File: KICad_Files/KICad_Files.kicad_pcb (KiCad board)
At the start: 2 copper layers, 30 x 34 mm, 48 parts, among them J1 Conn_01x03_Pin, J10 Conn_01x03_MountingPin, J2 Conn_01x03_Pin, J3 Conn_01x06, J4 Conn_01x06, J5 Conn_01x03_Pin, J6 Conn_01x02_Pin, J7 USB_C_Receptacle_USB2.0_16P, J8 Conn_01x03_MountingPin, J9 Conn_01x03_MountingPin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

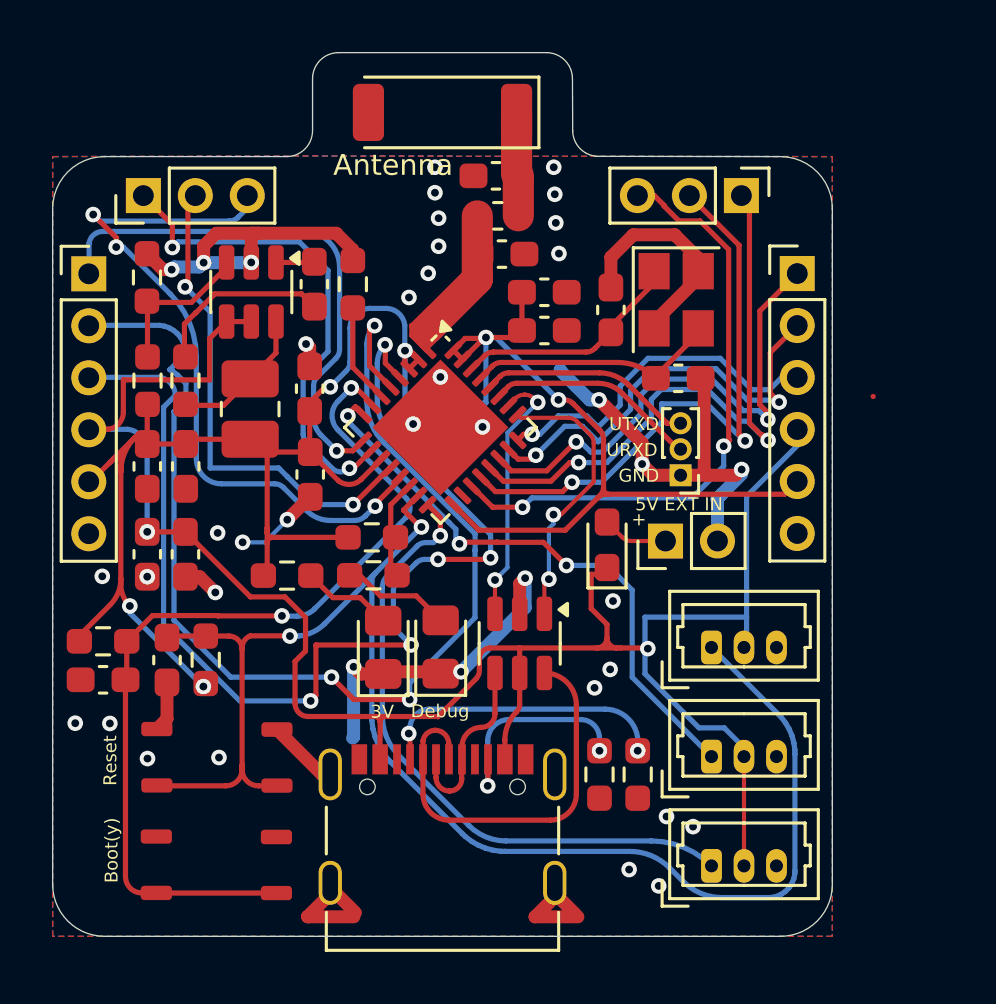
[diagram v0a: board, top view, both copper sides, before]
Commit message: Changed from 3 to 2 connector because of ESP32-C3 Limitations
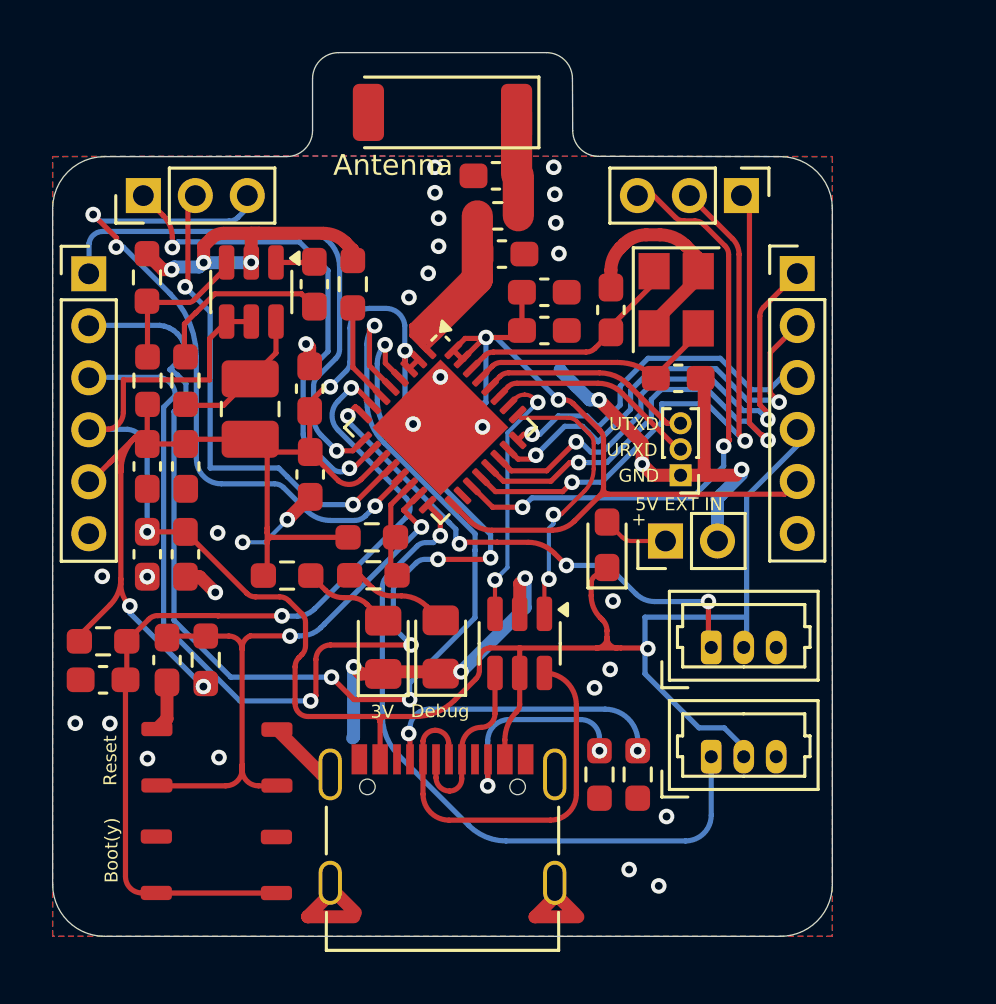
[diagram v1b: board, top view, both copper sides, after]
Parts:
- removed J8: Conn_01x03_MountingPin, Connector_Molex:Molex_PicoBlade_53047-0310_1x03_P1.25mm_Vertical
- moved J9 4.20 mm to (117.1, 103.3)
- moved J10 4.20 mm to (117.1, 107.5)
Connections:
- net /LED3 renamed /Boot
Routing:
- net /Boot: track 60.0 -> 24.3 mm
- net +5V: track 79.1 -> 73.9 mm
- net /LED2: track 22.9 -> 20.0 mm, vias 3 -> 4
- net /LED1: track 24.7 -> 27.2 mm
- net GND: track 74.1 -> 73.8 mm, vias 40 -> 39
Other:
- board text removed: "GPIO9"

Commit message: Switched the pi-filter components to 0402 size and changed the values
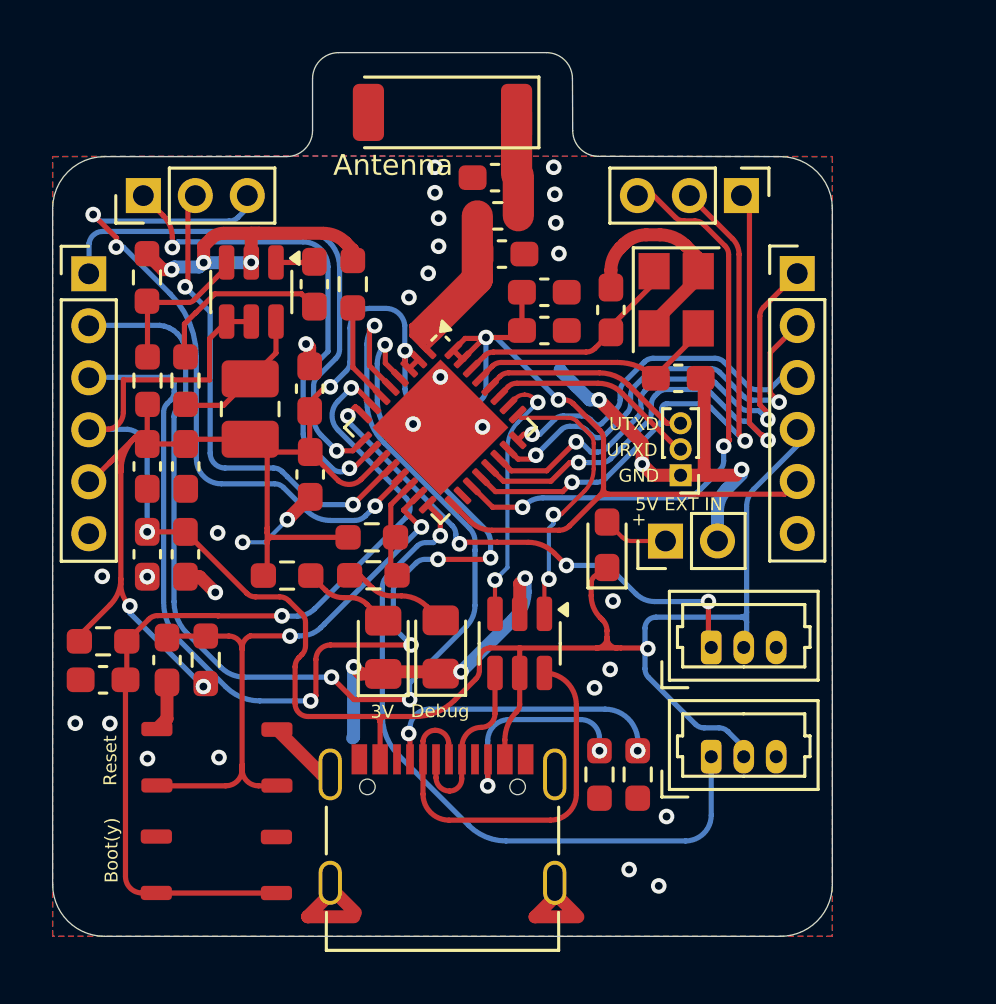
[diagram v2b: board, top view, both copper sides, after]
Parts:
- moved C4 0.08 mm to (108.8, 85.2)
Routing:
- net /GPIO 1: track 45.8 -> 44.9 mm

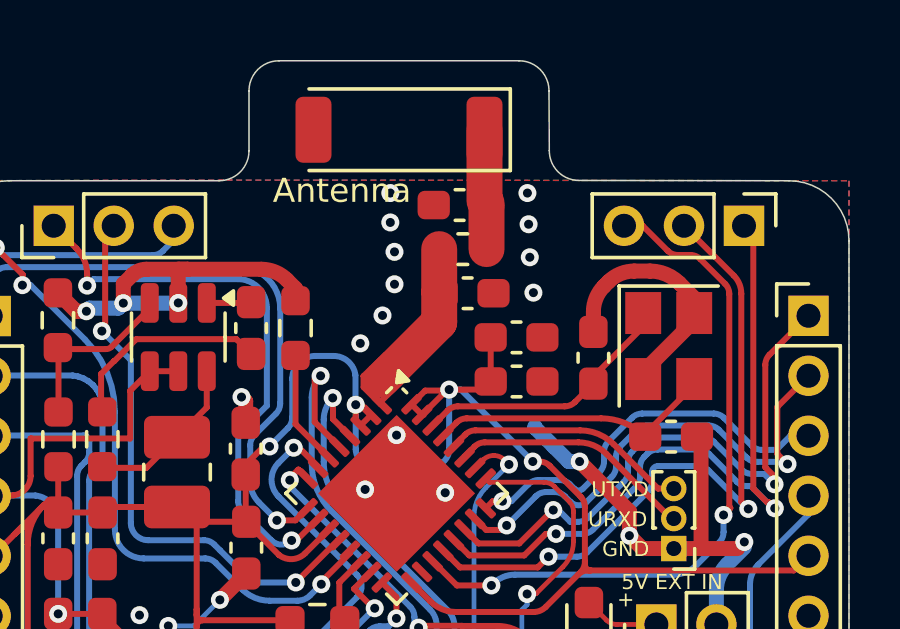
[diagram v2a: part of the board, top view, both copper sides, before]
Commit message: Switched crystal size and changed GPIO02 to be pulled high instead of low
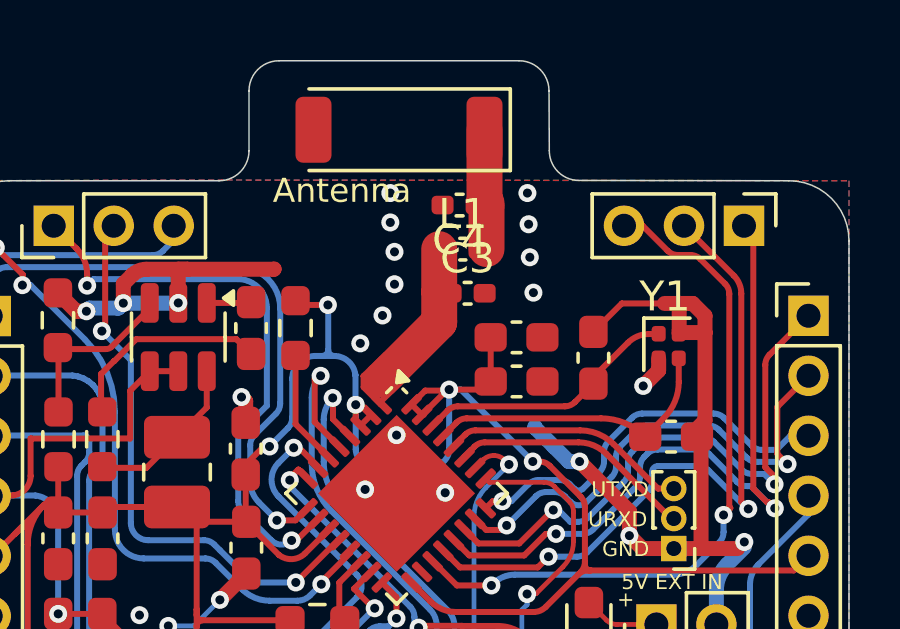
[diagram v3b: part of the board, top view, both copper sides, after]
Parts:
- C3, C4: value 3p3 -> 1p2; footprint Capacitor_SMD:C_0603_1608Metric_Pad1.08x0.95mm_HandSolder -> Capacitor_SMD:C_0402_1005Metric_Pad0.74x0.62mm_HandSolder
- L1: value 2n2 -> 3n9; footprint Inductor_SMD:L_0603_1608Metric -> Inductor_SMD:L_0402_1005Metric_Pad0.77x0.64mm_HandSolder
- Y1: footprint Crystal:Crystal_SMD_3225-4Pin_3.2x2.5mm -> Crystal:Crystal_SMD_1210-4Pin_1.2x1.0mm
- turned Y1 to 0 degrees
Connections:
- R6 pad 1: GND -> +3.3V
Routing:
- net +3.3V: track 88.1 -> 91.4 mm, vias 6 -> 7
- net GND: track 73.4 -> 74.5 mm, vias 39 -> 40

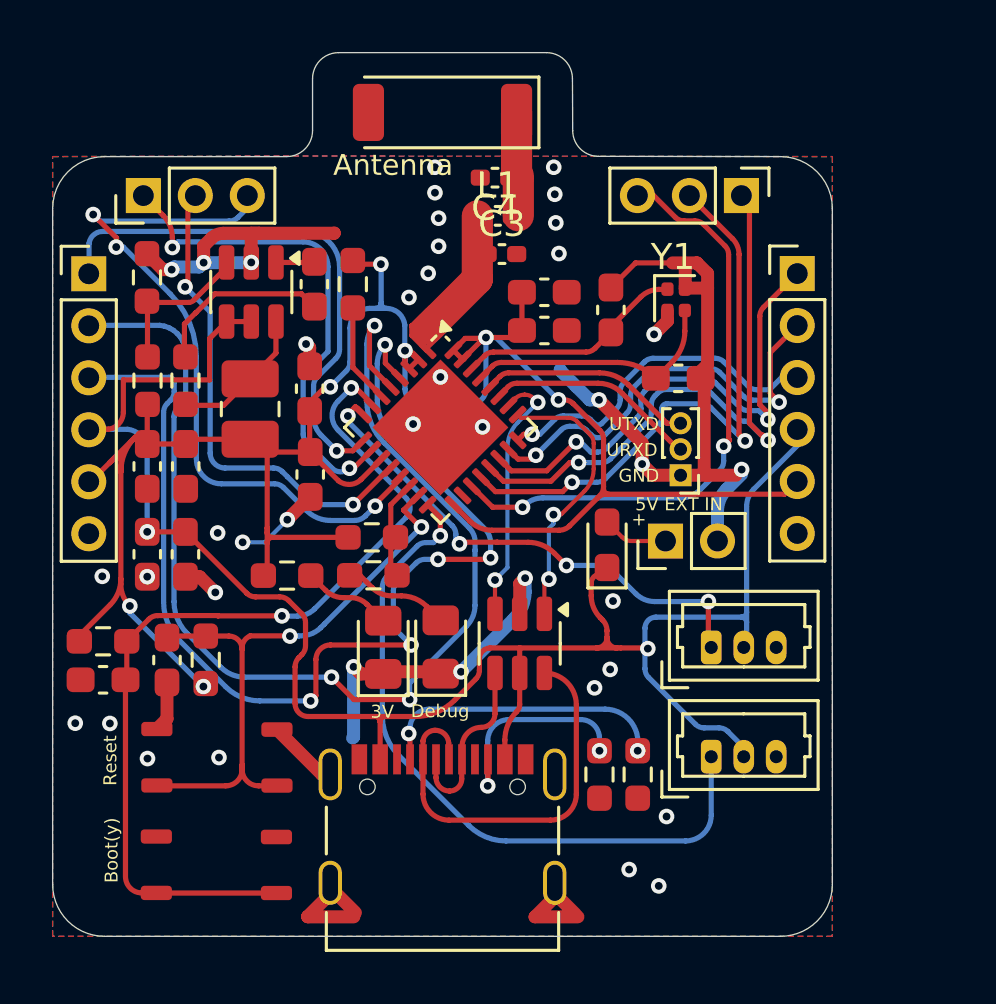
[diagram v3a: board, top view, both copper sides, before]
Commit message: fixed ground plane issues with the antenna
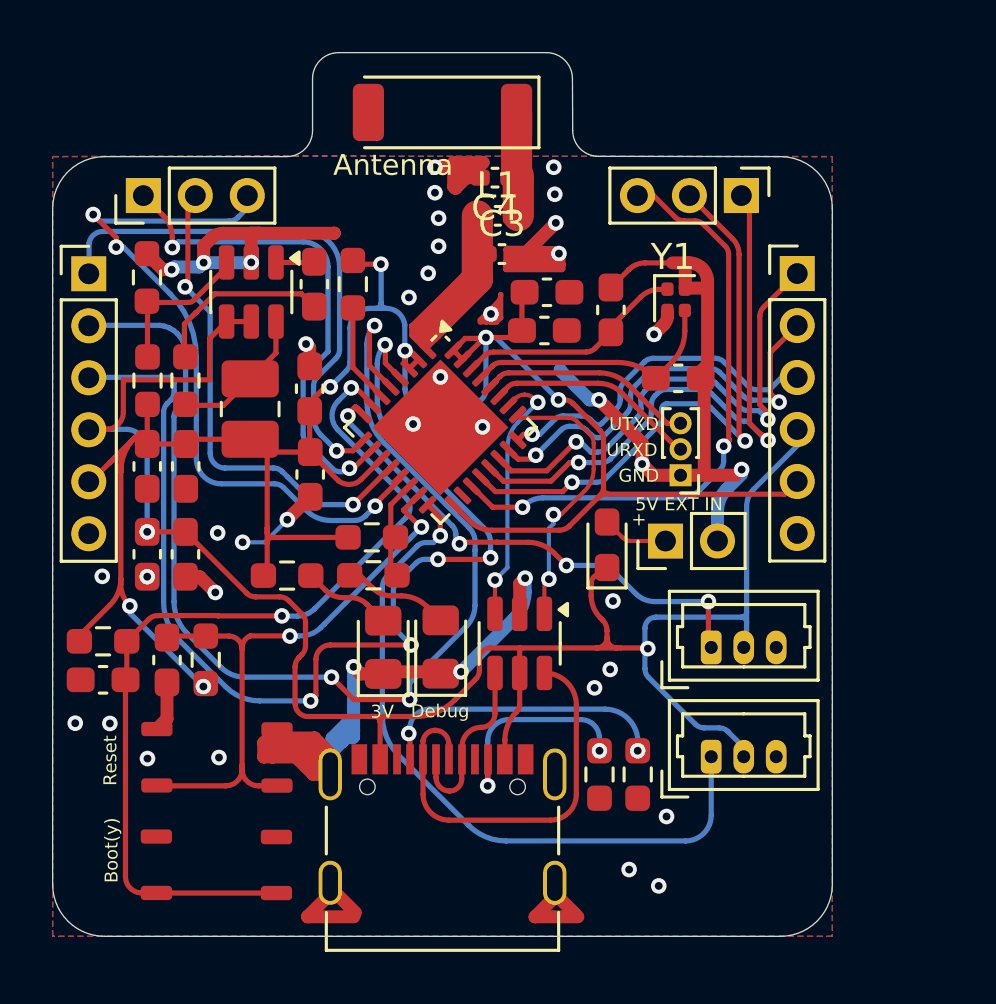
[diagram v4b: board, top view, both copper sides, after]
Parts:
- moved C10 0.10 mm to (110.8, 89.6)
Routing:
- net GND: track 74.5 -> 119.8 mm, vias 40 -> 41
